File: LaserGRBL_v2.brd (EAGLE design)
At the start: 91.7 x 58.7 mm, 19 parts

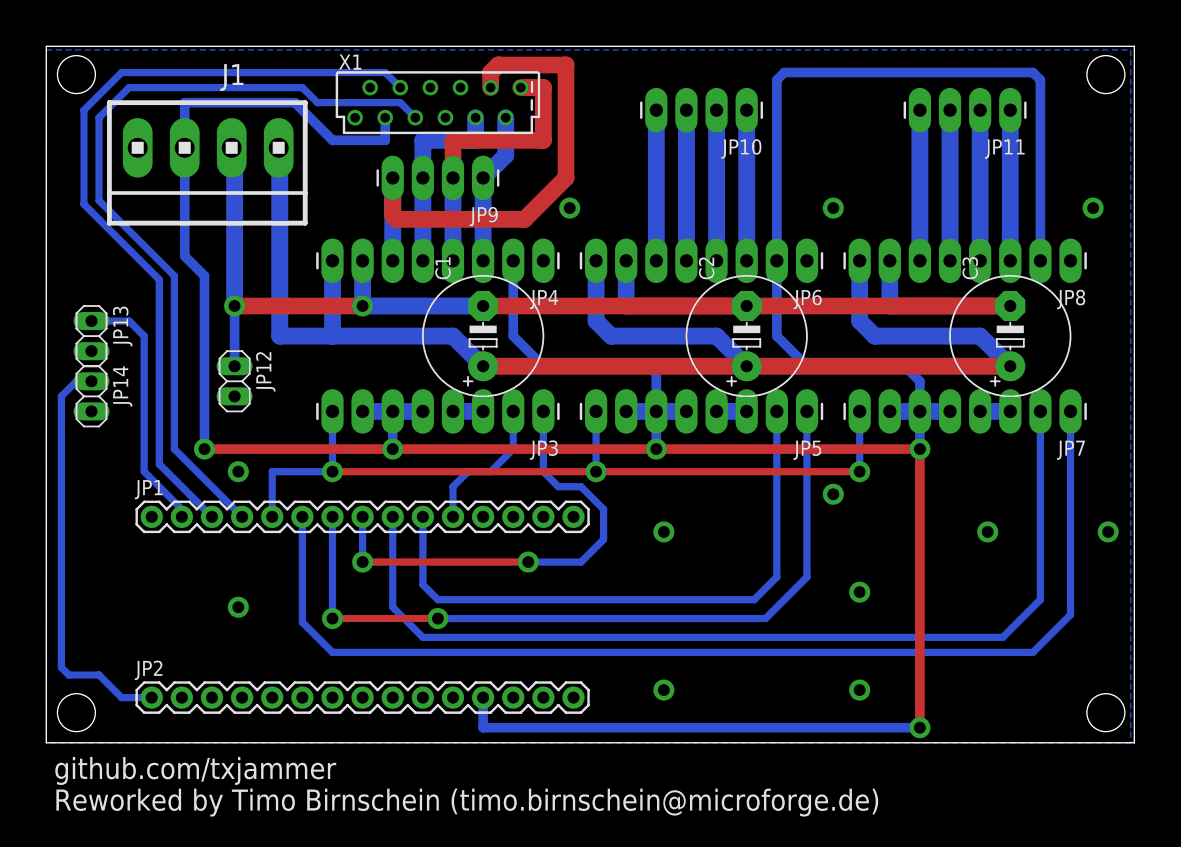
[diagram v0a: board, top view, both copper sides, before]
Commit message: Some changes to the board file to make it manufacturable.
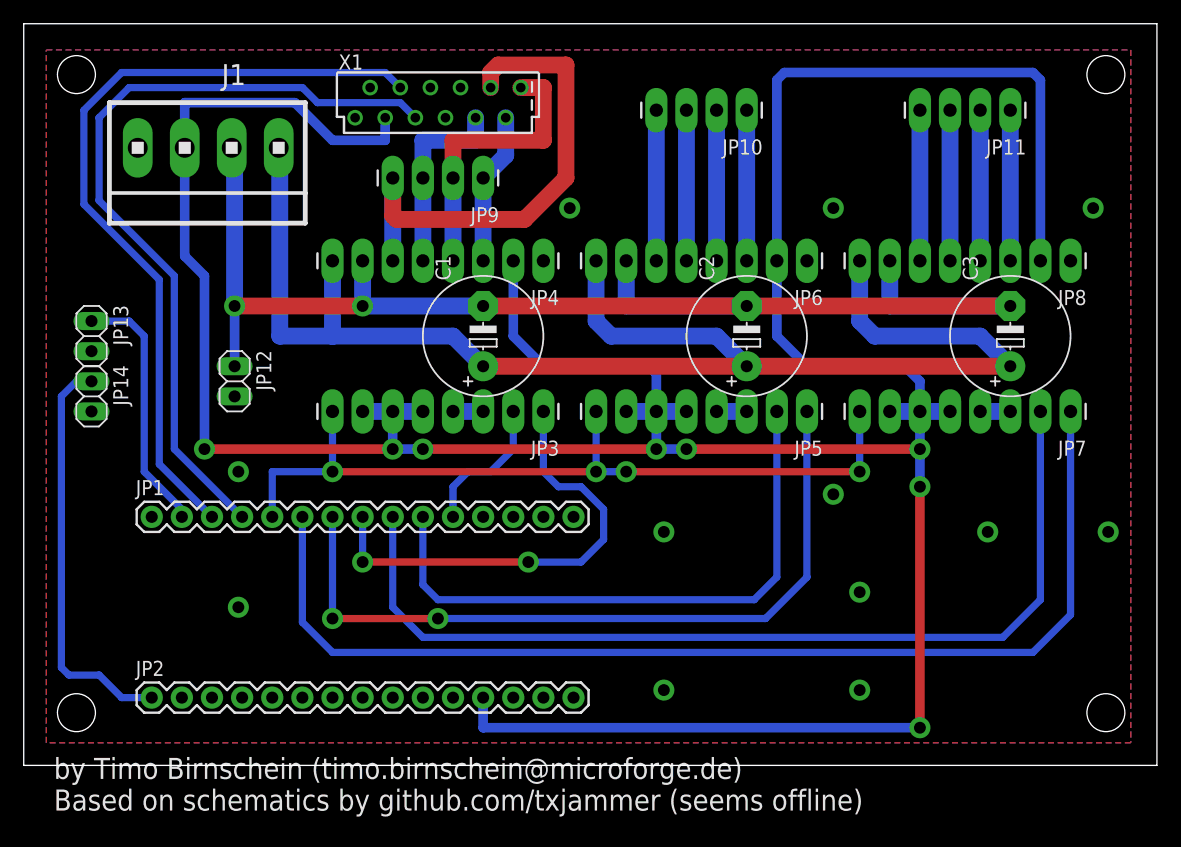
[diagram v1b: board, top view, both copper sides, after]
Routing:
- net 5V: vias 5 -> 8
- net DISABLE: vias 3 -> 4
- added copper zone on layer 1, net GND
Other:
- board size 91.7 x 58.7 mm -> 95.5 x 62.5 mm
- board text added: "by Timo Birnschein (timo.birnschein@microforge.de) Based on schematics by github.com/txjammer (seems offline)"
- board text removed: "github.com/txjammer Reworked by Timo Birnschein (timo.birnschein@microforge.de)"
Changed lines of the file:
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@@
 <board>
 <plain>
-<wire x1="0" y1="0" x2="91.7375" y2="0" width="0" layer="46"/>
-<wire x1="91.7375" y1="0" x2="91.7375" y2="58.725" width="0" layer="46"/>
-<wire x1="91.7375" y1="58.725" x2="0" y2="58.725" width="0" layer="46"/>
-<wire x1="0" y1="58.725" x2="0" y2="0" width="0" layer="46"/>
-<text x="0.635" y="-5.715" size="1.778" layer="25">github.com/txjammer
-Reworked by Timo Birnschein (timo.birnschein@microforge.de)</text>
+<wire x1="-1.905" y1="-1.905" x2="93.6425" y2="-1.905" width="0" layer="46"/>
+<wire x1="93.6425" y1="-1.905" x2="93.6425" y2="60.63" width="0" layer="46"/>
+<wire x1="93.6425" y1="60.63" x2="-1.905" y2="60.63" width="0" layer="46"/>
+<wire x1="-1.905" y1="60.63" x2="-1.905" y2="-1.905" width="0" layer="46"/>
+<text x="0.635" y="-5.715" size="1.778" layer="25">by Timo Birnschein (timo.birnschein@microforge.de)
+Based on schematics by github.com/txjammer (seems offline)</text>
 <hole x="2.54" y="56.34" drill="3.2"/>
 <hole x="89.34" y="56.34" drill="3.2"/>
@@
 <wire x1="36.83" y1="1.27" x2="73.66" y2="1.27" width="0.8128" layer="16"/>
 <via x="73.66" y="1.27" extent="1-16" drill="1" diameter="1.778" shape="octagon"/>
-<wire x1="73.66" y1="1.27" x2="73.66" y2="24.765" width="0.8128" layer="1"/>
 <wire x1="61.595" y1="40.64" x2="61.595" y2="34.29" width="0.8128" layer="16"/>
 <wire x1="61.595" y1="34.29" x2="64.135" y2="31.75" width="0.8128" layer="16"/>
@@
 <wire x1="72.39" y1="31.75" x2="73.66" y2="30.48" width="0.8128" layer="16"/>
 <wire x1="73.66" y1="30.48" x2="73.66" y2="27.94" width="0.8128" layer="16"/>
-<wire x1="29.21" y1="24.765" x2="51.435" y2="24.765" width="0.8128" layer="1"/>
-<wire x1="73.66" y1="24.765" x2="51.435" y2="24.765" width="0.8128" layer="1"/>
+<wire x1="73.66" y1="24.765" x2="73.66" y2="21.59" width="0.8128" layer="16"/>
+<via x="73.66" y="21.59" extent="1-16" drill="1" diameter="1.778" shape="octagon"/>
+<wire x1="73.66" y1="21.59" x2="73.66" y2="1.27" width="0.8128" layer="1"/>
+<wire x1="51.435" y1="24.765" x2="53.975" y2="24.765" width="0.8128" layer="16"/>
+<via x="53.975" y="24.765" extent="1-16" drill="1" diameter="1.778" shape="octagon"/>
+<wire x1="53.975" y1="24.765" x2="73.66" y2="24.765" width="0.8128" layer="1"/>
+<wire x1="29.21" y1="24.765" x2="31.75" y2="24.765" width="0.8128" layer="16"/>
+<via x="31.75" y="24.765" extent="1-16" drill="1" diameter="1.778" shape="octagon"/>
+<wire x1="31.75" y1="24.765" x2="51.435" y2="24.765" width="0.8128" layer="1"/>
 </signal>
 <signal name="GND">
@@
 <via x="16.1925" y="11.43" extent="1-16" drill="1" diameter="1.778" shape="octagon"/>
 <via x="16.1925" y="22.86" extent="1-16" drill="1" diameter="1.778" shape="octagon"/>
-<wire x1="52.07" y1="4.445" x2="52.07" y2="17.78" width="0" layer="19" extent="1-1"/>
-<wire x1="68.58" y1="12.7" x2="68.58" y2="4.445" width="0" layer="19" extent="1-1"/>
-<wire x1="16.1925" y1="22.86" x2="16.1925" y2="11.43" width="0" layer="19" extent="1-1"/>
-<wire x1="64.135" y1="40.64" x2="66.3575" y2="20.955" width="0" layer="19" extent="1-1"/>
+<polygon width="0.8128" layer="1" isolate="0.5334" orphans="yes" rank="6">
+<vertex x="0" y="58.42"/>
+<vertex x="91.44" y="58.42"/>
+<vertex x="91.44" y="0"/>
+<vertex x="0" y="0"/>
+</polygon>
 </signal>
 <signal name="YDIR">
@@
 <wire x1="46.355" y1="22.86" x2="24.13" y2="22.86" width="0.6096" layer="1"/>
 <via x="24.13" y="22.86" extent="1-16" drill="1" diameter="1.778" shape="octagon"/>
-<wire x1="46.355" y1="22.86" x2="68.58" y2="22.86" width="0.6096" layer="1"/>
 <via x="68.58" y="22.86" extent="1-16" drill="1" diameter="1.778" shape="octagon"/>
 <wire x1="68.58" y1="22.86" x2="68.58" y2="27.94" width="0.6096" layer="16"/>
+<wire x1="46.355" y1="22.86" x2="48.895" y2="22.86" width="0.6096" layer="16"/>
+<via x="48.895" y="22.86" extent="1-16" drill="1" diameter="1.778" shape="octagon"/>
+<wire x1="48.895" y1="22.86" x2="68.58" y2="22.86" width="0.6096" layer="1"/>
 </signal>
 <signal name="LASER_PWM">
